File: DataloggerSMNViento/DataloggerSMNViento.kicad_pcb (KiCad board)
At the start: 2 copper layers, 85.7 x 137.2 mm, 46 parts, among them J1 Screw_Terminal_01x03, J2 Screw_Terminal_01x02, J3 Vcc 5V SD, J4 GND SD, Q1 2N7000, Q2 2N7000, Q3 2N7000, U1 MAX485E, U2 w5100_module, U3 LM2596S-HW-319-v6_module, U5 LM358

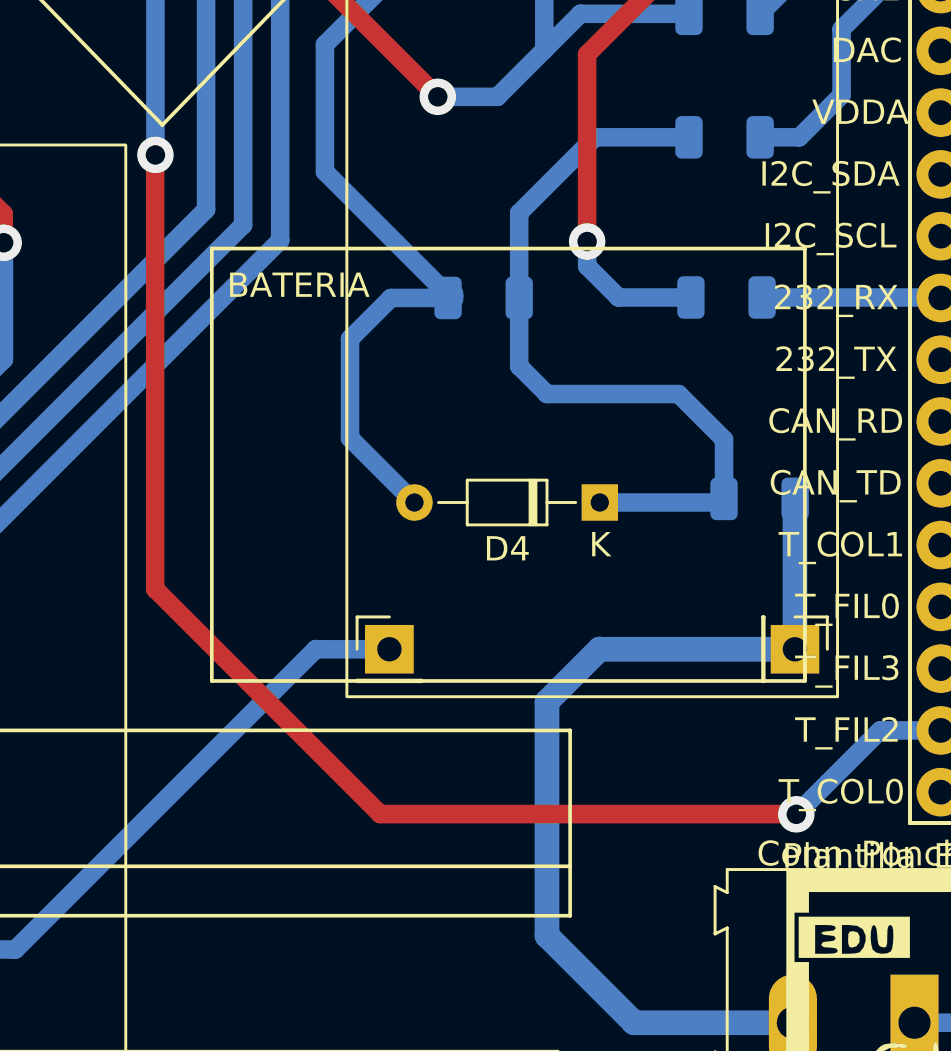
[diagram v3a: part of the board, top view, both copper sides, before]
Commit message: Se cambio el diodo zener de SMD a THT
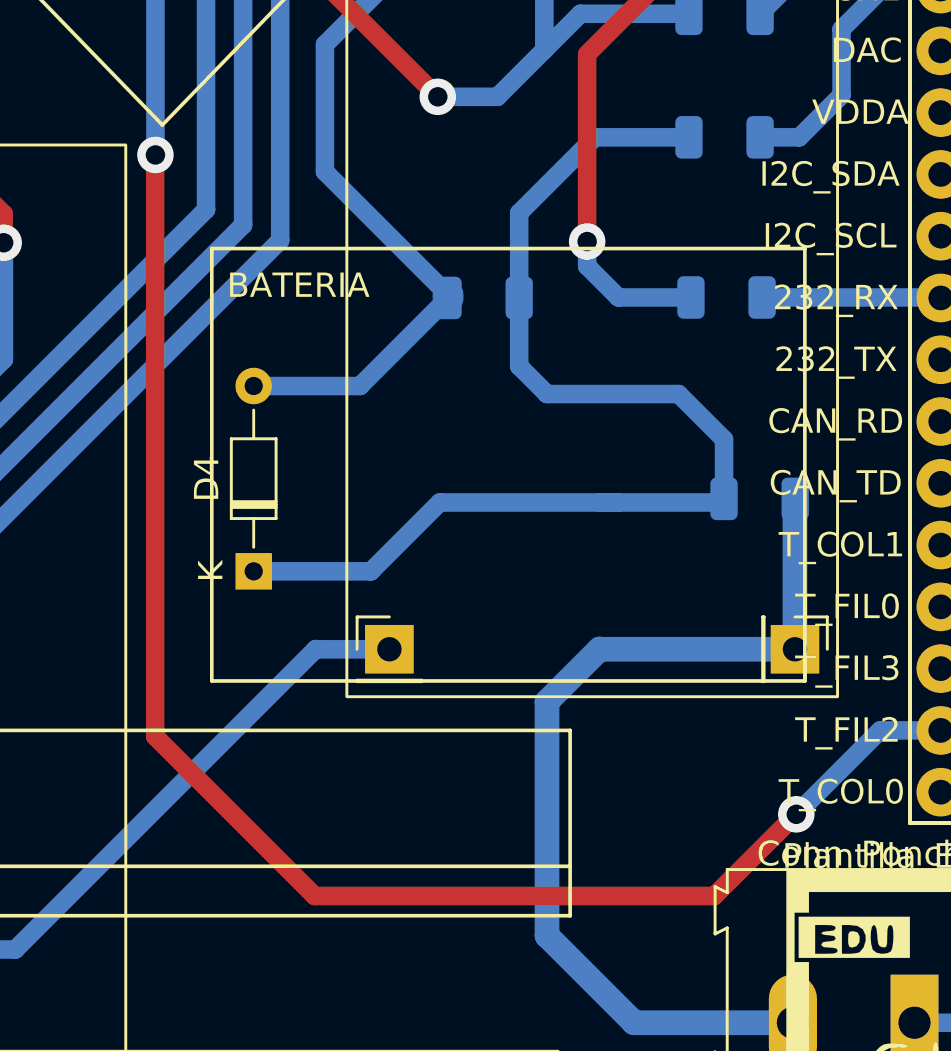
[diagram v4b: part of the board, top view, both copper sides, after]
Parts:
- moved D4 14.5 mm to (122.9, 128.1), turned to 90 degrees
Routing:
- net Net-(D4-Pad1): track 32.0 -> 48.2 mm
- net /Conector del Poncho/F2: track 108.9 -> 115.2 mm
- net GNDA: track 107.3 -> 104.3 mm
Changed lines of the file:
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@@
   )
   (footprint "Diode_THT:D_DO-34_SOD68_P7.62mm_Horizontal" (layer "F.Cu")
-    (at 137.11 125.25 180)
+    (at 122.88 128.08 90)
     (descr "Diode, DO-34_SOD68 series, Axial, Horizontal, pin pitch=7.62mm, , length*diameter=3.04*1.6mm^2, , https://www.nxp.com/docs/en/data-sheet/KTY83_SER.pdf")
     (tags "Diode DO-34_SOD68 series Axial Horizontal pin pitch 7.62mm  length 3.04mm diameter 1.6mm")
@@
     (property "Sheetname" "Power Supply")
     (attr through_hole)
-    (fp_text reference "D4" (at 3.81 -1.92) (layer "F.SilkS")
-      (effects (font (size 1 1) (thickness 0.15)))
-    )
-    (fp_text value "D_Zener" (at 3.81 1.92) (layer "F.Fab")
-      (effects (font (size 1 1) (thickness 0.15)))
-    )
-    (fp_text user "K" (at 0 -1.75) (layer "F.SilkS")
-      (effects (font (size 1 1) (thickness 0.15)))
-    )
-    (fp_text user "K" (at 0 -1.75) (layer "F.Fab")
-      (effects (font (size 1 1) (thickness 0.15)))
-    )
-    (fp_text user "${REFERENCE}" (at 4.038 0) (layer "F.Fab")
+    (fp_text reference "D4" (at 3.81 -1.92 90) (layer "F.SilkS")
+      (effects (font (size 1 1) (thickness 0.15)))
+    )
+    (fp_text value "D_Zener" (at 3.81 1.92 90) (layer "F.Fab")
+      (effects (font (size 1 1) (thickness 0.15)))
+    )
+    (fp_text user "K" (at 0 -1.75 90) (layer "F.SilkS")
+      (effects (font (size 1 1) (thickness 0.15)))
+    )
+    (fp_text user "K" (at 0 -1.75 90) (layer "F.Fab")
+      (effects (font (size 1 1) (thickness 0.15)))
+    )
+    (fp_text user "${REFERENCE}" (at 4.038 0 90) (layer "F.Fab")
       (effects (font (size 0.608 0.608) (thickness 0.0912)))
     )
@@
     (fp_line (start 2.29 -0.8) (end 2.29 0.8) (layer "F.Fab") (width 0.1))
     (fp_line (start 2.29 0.8) (end 5.33 0.8) (layer "F.Fab") (width 0.1))
-    (pad "1" thru_hole rect (at 0 0 180) (size 1.5 1.5) (drill 0.75) (layers *.Cu *.Mask)
+    (pad "1" thru_hole rect (at 0 0 90) (size 1.5 1.5) (drill 0.75) (layers *.Cu *.Mask)
       (net 7 "Net-(D4-Pad1)") (pinfunction "K") (pintype "passive"))
-    (pad "2" thru_hole oval (at 7.62 0 180) (size 1.5 1.5) (drill 0.75) (layers *.Cu *.Mask)
+    (pad "2" thru_hole oval (at 7.62 0 90) (size 1.5 1.5) (drill 0.75) (layers *.Cu *.Mask)
       (net 1 "GNDA") (pinfunction "A") (pintype "passive"))
     (model "${KICAD6_3DMODEL_DIR}/Diode_THT.3dshapes/D_DO-34_SOD68_P7.62mm_Horizontal.wrl"
@@
   (segment (start 130.8715 116.84) (end 130.8715 116.7115) (width 1.27) (layer "B.Cu") (net 1))
   (segment (start 125.81 111.65) (end 125.81 106.42) (width 0.762) (layer "B.Cu") (net 1))
-  (segment (start 126.84 122.6) (end 126.84 118.524) (width 0.762) (layer "B.Cu") (net 1))
   (segment (start 131.862 96.774) (end 131.862 102.8445) (width 0.762) (layer "B.Cu") (net 1))
   (segment (start 138.98 89.52) (end 145.57 89.52) (width 0.762) (layer "B.Cu") (net 1))
-  (segment (start 130.8715 116.84) (end 128.524 116.84) (width 0.762) (layer "B.Cu") (net 1))
-  (segment (start 129.49 125.25) (end 126.84 122.6) (width 0.762) (layer "B.Cu") (net 1))
   (segment (start 155.94 87.31) (end 155.94 99.59) (width 0.762) (layer "B.Cu") (net 1))
   (segment (start 125.81 106.42) (end 129.36 102.87) (width 0.762) (layer "B.Cu") (net 1))
@@
   (segment (start 153.67 96.52) (end 151.13 96.52) (width 0.762) (layer "B.Cu") (net 1))
   (segment (start 145.57 89.52) (end 150.07 85.02) (width 0.762) (layer "B.Cu") (net 1))
-  (segment (start 126.84 118.524) (end 128.524 116.84) (width 0.762) (layer "B.Cu") (net 1))
+  (segment (start 122.88 120.46) (end 127.2515 120.46) (width 0.762) (layer "B.Cu") (net 1))
+  (segment (start 127.2515 120.46) (end 130.8715 116.84) (width 0.762) (layer "B.Cu") (net 1))
   (segment (start 133.76 86) (end 135.46 86) (width 0.762) (layer "B.Cu") (net 1))
   (segment (start 86.97 88.9) (end 92.03 93.96) (width 1.016) (layer "B.Cu") (net 2))
@@
   (segment (start 150.2675 43.89) (end 150.3175 43.94) (width 0.635) (layer "B.Cu") (net 6))
   (segment (start 136.906 110.236) (end 140.7775 110.236) (width 0.762) (layer "B.Cu") (net 7))
+  (segment (start 122.88 128.08) (end 127.7 128.08) (width 0.762) (layer "B.Cu") (net 7))
   (segment (start 133.7965 113.3455) (end 133.7965 116.84) (width 0.762) (layer "B.Cu") (net 7))
+  (segment (start 130.53 125.25) (end 137.87 125.25) (width 0.762) (layer "B.Cu") (net 7))
   (segment (start 142.0955 125.222) (end 142.2175 125.1) (width 0.762) (layer "B.Cu") (net 7))
   (segment (start 134.94 120.79) (end 133.7965 119.6465) (width 0.762) (layer "B.Cu") (net 7))
@@
   (segment (start 140.35 120.79) (end 134.94 120.79) (width 0.762) (layer "B.Cu") (net 7))
   (segment (start 142.0675 125.25) (end 142.2175 125.1) (width 0.508) (layer "B.Cu") (net 7))
-  (segment (start 137.11 125.25) (end 142.0675 125.25) (width 0.762) (layer "B.Cu") (net 7))
+  (segment (start 127.7 128.08) (end 130.53 125.25) (width 0.762) (layer "B.Cu") (net 7))
+  (segment (start 137.87 125.25) (end 142.0675 125.25) (width 0.762) (layer "B.Cu") (net 7))
   (segment (start 142.2175 125.1) (end 142.2175 122.6575) (width 0.762) (layer "B.Cu") (net 7))
+  (segment (start 137.11 125.25) (end 137.87 125.25) (width 0.762) (layer "B.Cu") (net 7))
   (segment (start 133.7965 119.6465) (end 133.7965 116.84) (width 0.762) (layer "B.Cu") (net 7))
   (segment (start 133.7965 113.3455) (end 136.906 110.236) (width 0.762) (layer "B.Cu") (net 7))
@@
   (segment (start 108.725 84.95) (end 111.02 87.245) (width 0.762) (layer "B.Cu") (net 10))
   (segment (start 107.455 79.41) (end 108.725 79.41) (width 0.635) (layer "B.Cu") (net 10))
-  (segment (start 118.83 128.81) (end 128.08 138.06) (width 0.762) (layer "F.Cu") (net 11))
+  (segment (start 118.83 134.87) (end 125.39 141.43) (width 0.762) (layer "F.Cu") (net 11))
+  (segment (start 125.39 141.43) (end 141.81 141.43) (width 0.762) (layer "F.Cu") (net 11))
   (segment (start 145.18 138.06) (end 145.19 138.07) (width 0.635) (layer "F.Cu") (net 11))
-  (segment (start 118.83 110.97) (end 118.83 128.81) (width 0.762) (layer "F.Cu") (net 11))
+  (segment (start 141.81 141.43) (end 145.18 138.06) (width 0.762) (layer "F.Cu") (net 11))
   (segment (start 118.83 110.97) (end 118.84 110.96) (width 1.016) (layer "F.Cu") (net 11))
-  (segment (start 128.08 138.06) (end 145.18 138.06) (width 0.762) (layer "F.Cu") (net 11))
+  (segment (start 118.83 110.97) (end 118.83 134.87) (width 0.762) (layer "F.Cu") (net 11))
   (via (at 118.84 110.96) (size 1.5) (drill 0.8) (layers "F.Cu" "B.Cu") (net 11))
   (via (at 145.19 138.07) (size 1.5) (drill 0.8) (layers "F.Cu" "B.Cu") (net 11))
@@
     (connect_pads (clearance 0.508))
     (min_thickness 0.254) (filled_areas_thickness no)
-    (fill yes (thermal_gap 0.508) (thermal_bridge_width 0.508))
+    (fill (thermal_gap 0.508) (thermal_bridge_width 0.508))
     (polygon
       (pts

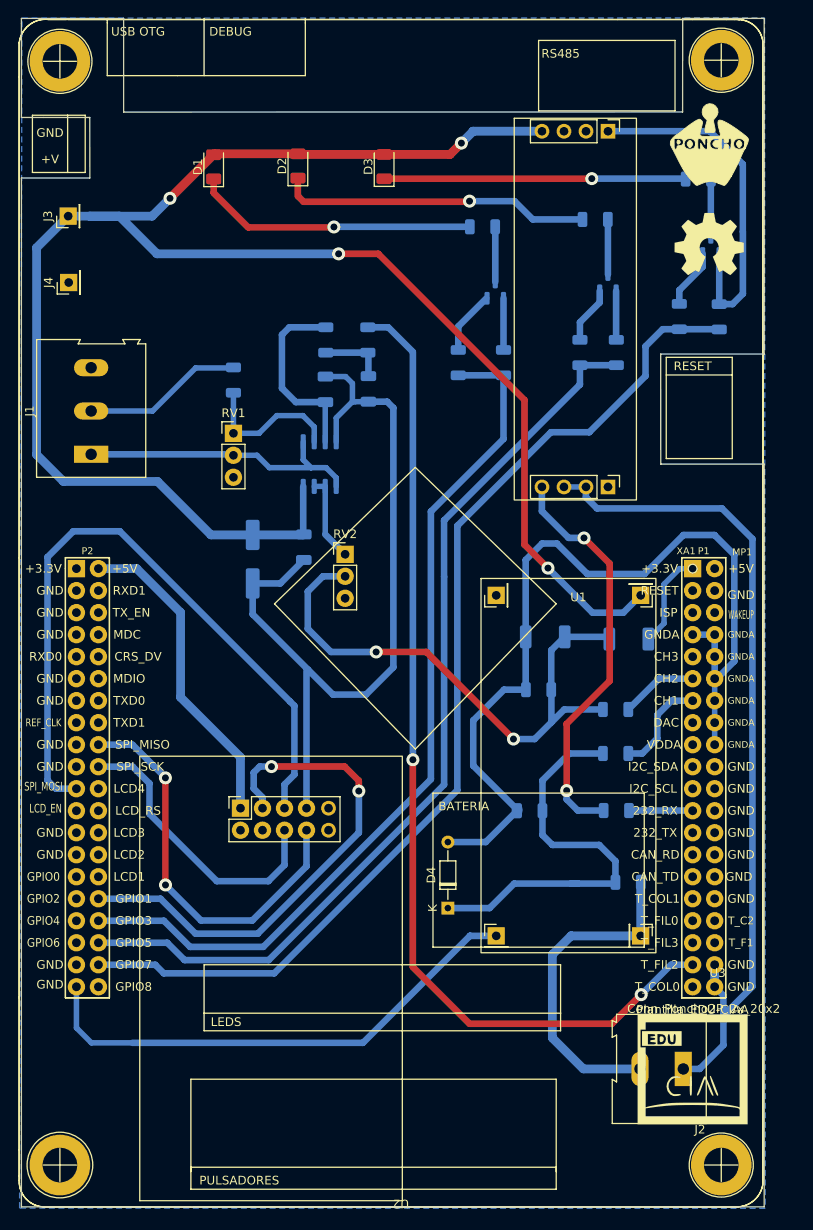
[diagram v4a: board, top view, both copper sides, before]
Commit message: Subo la version v1.2 THT de la poncho, para fabricar en el SMN
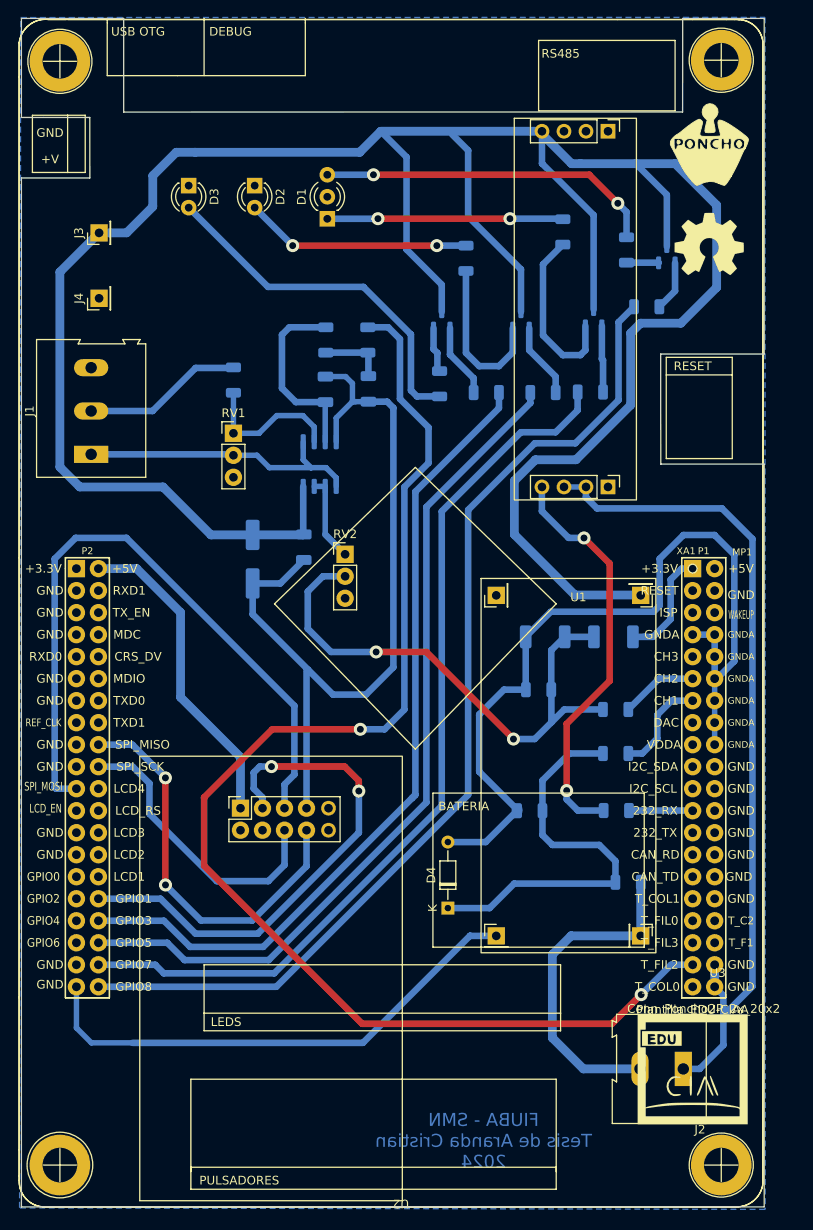
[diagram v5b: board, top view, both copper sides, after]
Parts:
- removed the D3 at (115.5, 42.5)
- removed R10: 680, Resistor_SMD:R_1206_3216Metric
- removed R8: 330K, Resistor_SMD:R_1206_3216Metric
- removed R9: 10K, Resistor_SMD:R_1206_3216Metric
- added D2: LED, LED_THT:LED_D3.0mm, F.Cu at (100.6, 44.7)
- added Q4: Q_NPN_BEC, Package_TO_SOT_SMD:SOT-23, B.Cu at (131.3, 60.2)
- added R14: 1k, Resistor_SMD:R_1206_3216Metric, B.Cu at (139.3, 68.5)
- added R20: 39, Resistor_SMD:R_1206_3216Metric, B.Cu at (136.1, 50.0)
- D1: value LED -> LED_Dual_AKA; footprint LED_SMD:LED_1206_3216Metric -> LED_THT:LED_D3.0mm-3
- D3: renamed from D2; footprint LED_SMD:LED_1206_3216Metric -> LED_THT:LED_D3.0mm
- Q1, Q2, Q3: value 2N7000 -> Q_NPN_BEC
- R2, R5: value 330K -> 39
- R3, R6: value 10K -> 1k
- R4: value 680 -> 1k
- R7: value 680 -> 39
- moved Q3 32.2 mm to (122.2, 60.2)
- moved R3 22.7 mm to (145.8, 58.7), turned to 0 degrees
- moved R5 20.7 mm to (121.9, 67.6)
- moved R2 19.3 mm to (143.5, 52.1), turned to 90 degrees
- moved R4 19.1 mm to (127.3, 68.6), turned to 180 degrees
- moved R7 15.6 mm to (125.0, 53.1), turned to 90 degrees
- moved D1 14.4 mm to (109.0, 48.5)
- moved D3 12.8 mm to (93.0, 44.7), turned to -90 degrees
- moved Q1 11.8 mm to (139.7, 59.9)
- moved Q2 7.53 mm to (148.2, 52.7)
- moved R6 6.29 mm to (133.9, 68.6), turned to 0 degrees
- moved J3 4.05 mm to (82.6, 50.1)
- moved J4 3.95 mm to (82.6, 57.7)
- moved D5 1.80 mm to (142.0, 96.8)
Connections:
- D1 pad 2: +5VP -> GNDinVariador
- D3 pad 1: Net-(D2-Pad1) -> GNDinVariador
- D3 pad 2: +5VP -> Net-(D3-Pad2)
- Q1 pad 1: GNDinVariador -> Net-(R14-Pad2)
- Q1 pad 2: Net-(Q1-Pad2) -> Net-(R20-Pad1)
- Q1 pad 3: Net-(Q1-Pad3) -> +5VP
- Q2 pad 1: GNDinVariador -> Net-(R3-Pad2)
- Q2 pad 2: Net-(Q2-Pad2) -> Net-(R2-Pad1)
- Q2 pad 3: Net-(Q2-Pad3) -> +5VP
- Q3 pad 1: GNDinVariador -> Net-(R4-Pad2)
- Q3 pad 2: Net-(Q3-Pad2) -> Net-(R5-Pad1)
- Q3 pad 3: Net-(Q3-Pad3) -> +5VP
- R2 pad 1: GNDinVariador -> Net-(R2-Pad1)
- R2 pad 2: /Conector del Poncho/GPIO3 -> Net-(D1-Pad3)
- R3 pad 1: /Conector del Poncho/GPIO3 -> /Conector del Poncho/GPIO8
- R3 pad 2: Net-(Q1-Pad2) -> Net-(R3-Pad2)
- R4 pad 1: Net-(D1-Pad1) -> /Conector del Poncho/GPIO3
- R4 pad 2: Net-(Q1-Pad3) -> Net-(R4-Pad2)
- R5 pad 1: GNDinVariador -> Net-(R5-Pad1)
- R5 pad 2: /Conector del Poncho/GPIO5 -> Net-(D3-Pad2)
- R6 pad 2: Net-(Q2-Pad2) -> Net-(R6-Pad2)
- R7 pad 1: Net-(D2-Pad1) -> Net-(R7-Pad1)
- R7 pad 2: Net-(Q2-Pad3) -> Net-(D2-Pad2)
- XA1 pad 80: unconnected-(XA1-Pad80) -> /Conector del Poncho/GPIO8
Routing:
- net /Conector del Poncho/GPIO8: track 0.00 -> 118.9 mm
- net +5VP: track 221.3 -> 300.1 mm, vias 4 -> 0
- net GNDinVariador: track 321.1 -> 268.3 mm
- net Net-(D3-Pad2): track 0.00 -> 41.8 mm
- net Net-(D1-Pad3): track 0.00 -> 39.2 mm, vias 0 -> 2
- net /Conector del Poncho/F2: track 115.2 -> 151.5 mm
- net Net-(D2-Pad1): track 36.1 -> 0.00 mm, vias 1 -> 0
- net Net-(D3-Pad1): track 34.8 -> 0.00 mm, vias 1 -> 0
- net Net-(D2-Pad2): track 0.00 -> 26.2 mm, vias 0 -> 2
- net Net-(R20-Pad1): track 0.00 -> 20.3 mm
- net Net-(R7-Pad1): track 0.00 -> 19.0 mm
- net /Conector del Poncho/GPIO7: track 122.7 -> 104.6 mm
- net /Conector del Poncho/GPIO5: track 108.2 -> 98.5 mm
- net Net-(R6-Pad2): track 0.00 -> 8.71 mm
- net Net-(R4-Pad2): track 0.00 -> 8.57 mm
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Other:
- board text added: "FIUBA - SMN Tesis de Aranda Cristian 2024"
